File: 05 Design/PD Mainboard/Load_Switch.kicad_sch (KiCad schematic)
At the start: 6 parts

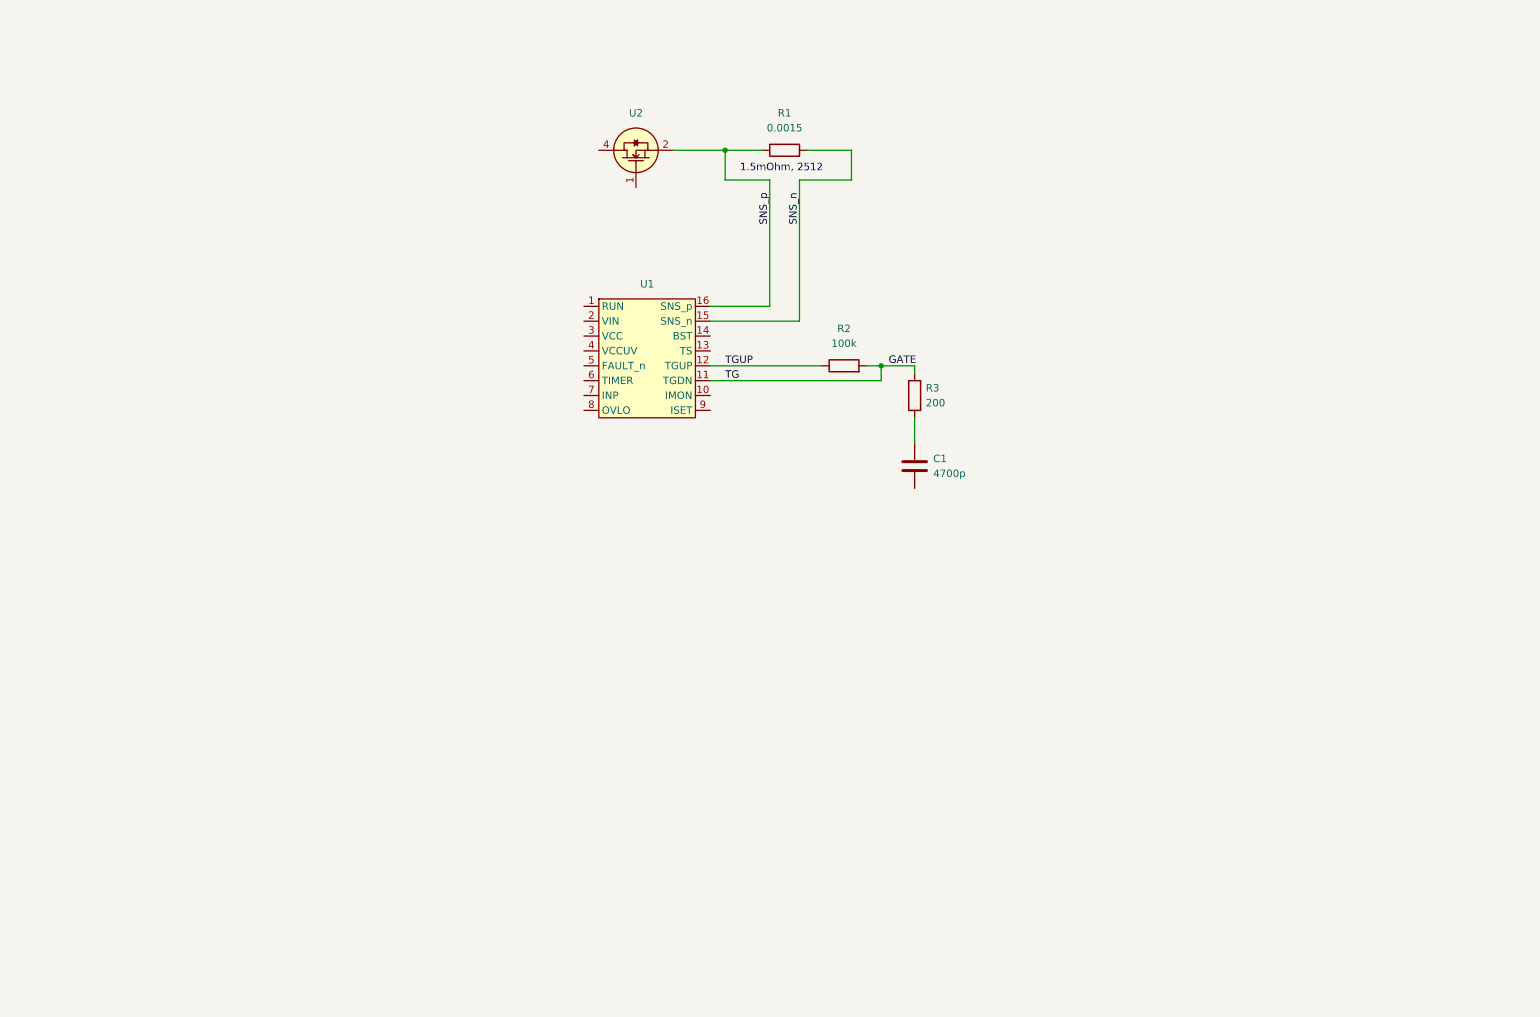
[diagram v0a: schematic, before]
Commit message: load switch with iso spi idea
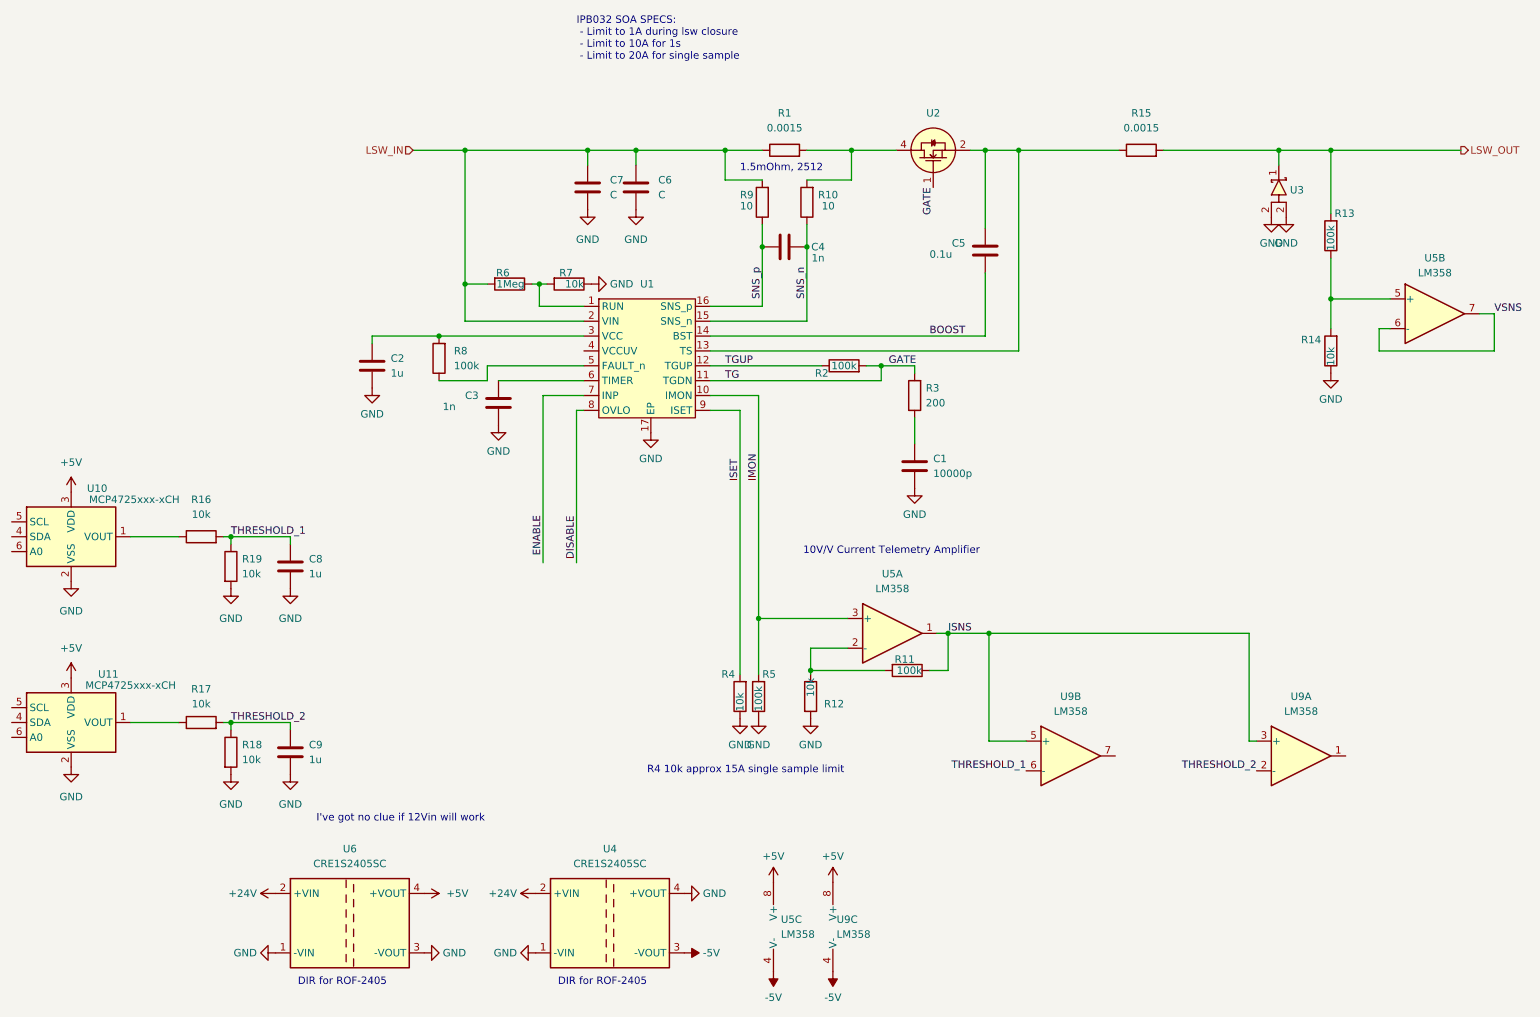
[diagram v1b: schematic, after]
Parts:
- added C2, C8, C9: 1u, Capacitor_THT:C_Disc_D3.4mm_W2.1mm_P2.50mm, symbol Device:C
- added C3, C4: 1n, Capacitor_THT:C_Disc_D3.4mm_W2.1mm_P2.50mm, symbol Device:C
- added C5: 0.1u, Capacitor_THT:C_Disc_D3.4mm_W2.1mm_P2.50mm, symbol Device:C
- added C6, C7: C, Capacitor_SMD:C_2220_5650Metric_Pad1.97x5.40mm_HandSolder, symbol Device:C
- added R10, R9: 10, Resistor_THT:R_Axial_DIN0204_L3.6mm_D1.6mm_P5.08mm_Horizontal, symbol Device:R
- added R11, R13, R5, R8: 100k, Resistor_THT:R_Axial_DIN0204_L3.6mm_D1.6mm_P5.08mm_Horizontal, symbol Device:R
- added R12, R14, R16, R17, R18, R19, R4, R7: 10k, Resistor_THT:R_Axial_DIN0204_L3.6mm_D1.6mm_P5.08mm_Horizontal, symbol Device:R
- added R15: 0.0015, Resistor_SMD:R_2512_6332Metric_Pad1.40x3.35mm_HandSolder, symbol Device:R
- added R6: 1Meg, Resistor_THT:R_Axial_DIN0204_L3.6mm_D1.6mm_P5.08mm_Horizontal, symbol Device:R
- added U10, U11: MCP4725xxx-xCH, Package_TO_SOT_SMD:SOT-23-6, symbol Analog_DAC:MCP4725xxx-xCH
- added U3: ~, Diode_SMD:D_PowerDI-5, symbol my parts:SBR12U100P5Q-13
- added U4, U6: CRE1S2405SC, Converter_DCDC:Converter_DCDC_Murata_CRE1xxxxxxSC_THT, symbol Regulator_Switching:CRE1S2405SC
- added U5, U9: LM358, Package_SO:SOIC-8_3.9x4.9mm_P1.27mm, symbol Amplifier_Operational:LM358
- C1: value 4700p -> 10000p
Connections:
- net GATE: now also U2.1
- net SNS_n: now also C4.2, R10.1; no longer R1.2
- net SNS_p: now also C4.1, R9.1; no longer R1.1, U2.2, U2.3, U2.5, U2.6, U2.7
- net at U1.1 (RUN): now also R6.1, R7.2
- net IMON: now reaches U1.10 (IMON)
- net IMON: now also R5.2, U5.3 (+)
- net at U1.13 (TS): now also U2.2, U2.3, U2.5, U2.6, U2.7, C5.1, R15.1
- net BOOST: now reaches U1.14 (BST)
- net BOOST: now also C5.2
- net LSW_IN: now reaches U1.2 (VIN)
- net LSW_IN: now also R1.1, C6.1, C7.1, R6.2, R9.2
- net at U1.3 (VCC): now also C2.1, R8.2
- net at U1.5 (FAULT_n): now also R8.1
- net at U1.6 (TIMER): now also C3.1
- net ENABLE: now reaches U1.7 (INP)
- net DISABLE: now reaches U1.8 (OVLO)
- net ISET: now reaches U1.9 (ISET)
- net ISET: now also R4.2
- net at U2.4: now also R1.2, R10.2
- net GND: now reaches C1.2
- net GND: now also U1.17 (EP), C2.2, C3.2, C6.2, C7.2, C8.2, C9.2, R12.2, R14.1, R18.2, R19.2, R4.1, R5.1, R7.1, U10.2 (VSS), U11.2 (VSS), U3.2, U4.1 (-VIN), U4.4 (+VOUT), U6.1 (-VIN), U6.3 (-VOUT)
- new net: R13.1, R14.2, U5.5 (+)
- new net: R16.1, U10.1 (VOUT)
- new net: R11.2, R12.1, U5.2 (-)
- new net: R17.1, U11.1 (VOUT)
- new net +24V: U4.2 (+VIN), U6.2 (+VIN)
- new net +5V: U10.3 (VDD), U11.3 (VDD), U5.8 (V+), U6.4 (+VOUT), U9.8 (V+)
- new net -5V: U4.3 (-VOUT), U5.4 (V-), U9.4 (V-)
- new net ISNS: R11.1, U5.1, U9.3 (+), U9.5 (+)
- new net LSW_OUT: R13.2, R15.2, U3.1
- new net THRESHOLD_1: C8.1, R16.2, R19.1, U9.6 (-)
- new net THRESHOLD_2: C9.1, R17.2, R18.1, U9.2 (-)
- new net VSNS: U5.6 (-), U5.7
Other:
- note added: "10V/V Current Telemetry Amplifier"
- note added: "DIR for ROF-2405"
- note added: "I've got no clue if 12Vin will work"
- note added: "IPB032 SOA SPECS: - Limit to 1A during lsw closure - Limit to 10A for 1s - Limit to 20A for single sample"
- note added: "R4 10k approx 15A single sample limit"
